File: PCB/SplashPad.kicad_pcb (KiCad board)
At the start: 2 copper layers, 67 x 83 mm, 58 parts, among them SW1 SW_Push_45deg, SW10 RotaryEncoder_Switch, SW2 SW_Push_45deg, SW3 SW_Push_45deg, SW4 SW_Push_45deg, SW5 SW_Push_45deg, SW6 SW_Push_45deg, SW7 SW_Push_45deg, SW8 SW_Push_45deg, SW9 SW_Push_45deg, U1 XIAO-RP2040-DIP

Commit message: Final Updates
This is the last one I swear
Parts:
- moved G*** 2.50 mm to (158.0, 146.5)
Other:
- board text added: "SplashPad"

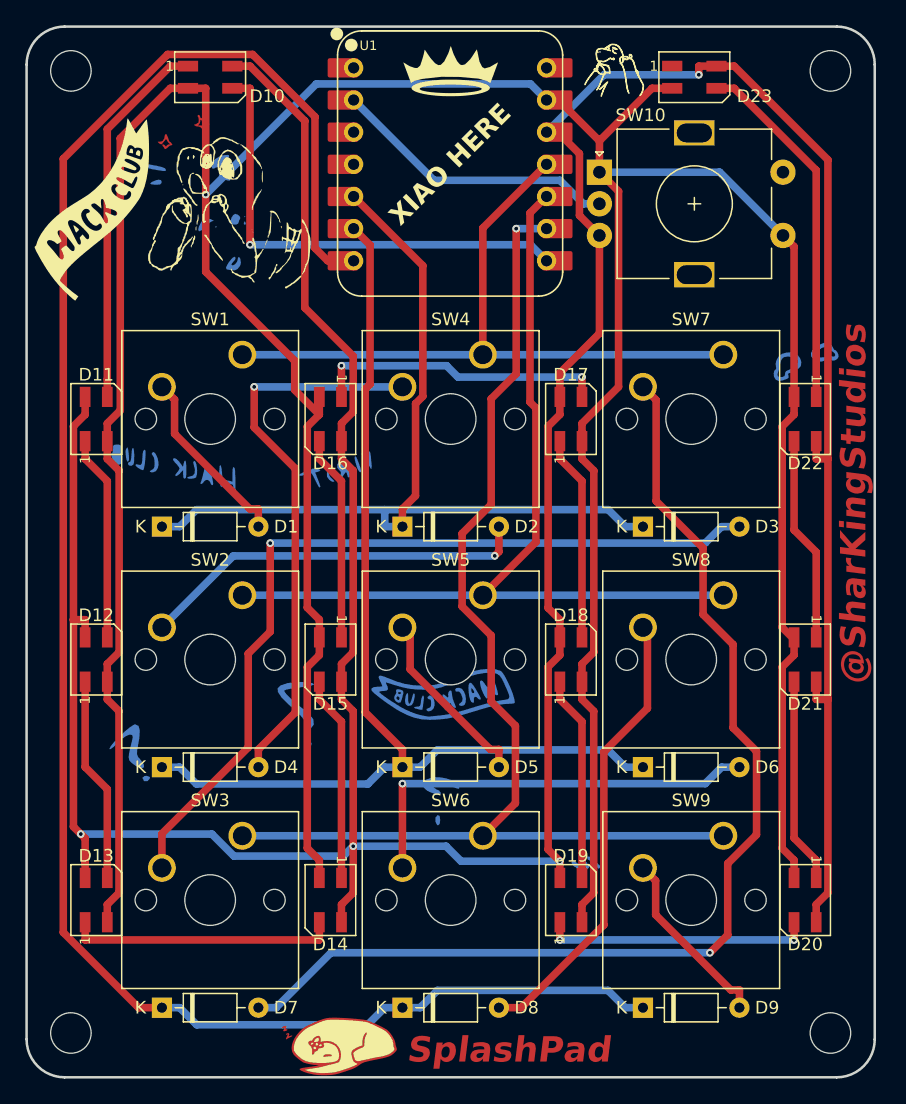
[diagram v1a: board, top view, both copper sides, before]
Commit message: LED Voltage Fix
I thought they worked at 3.3v oopsies
I also had the encoder wired wrong and fixed that.
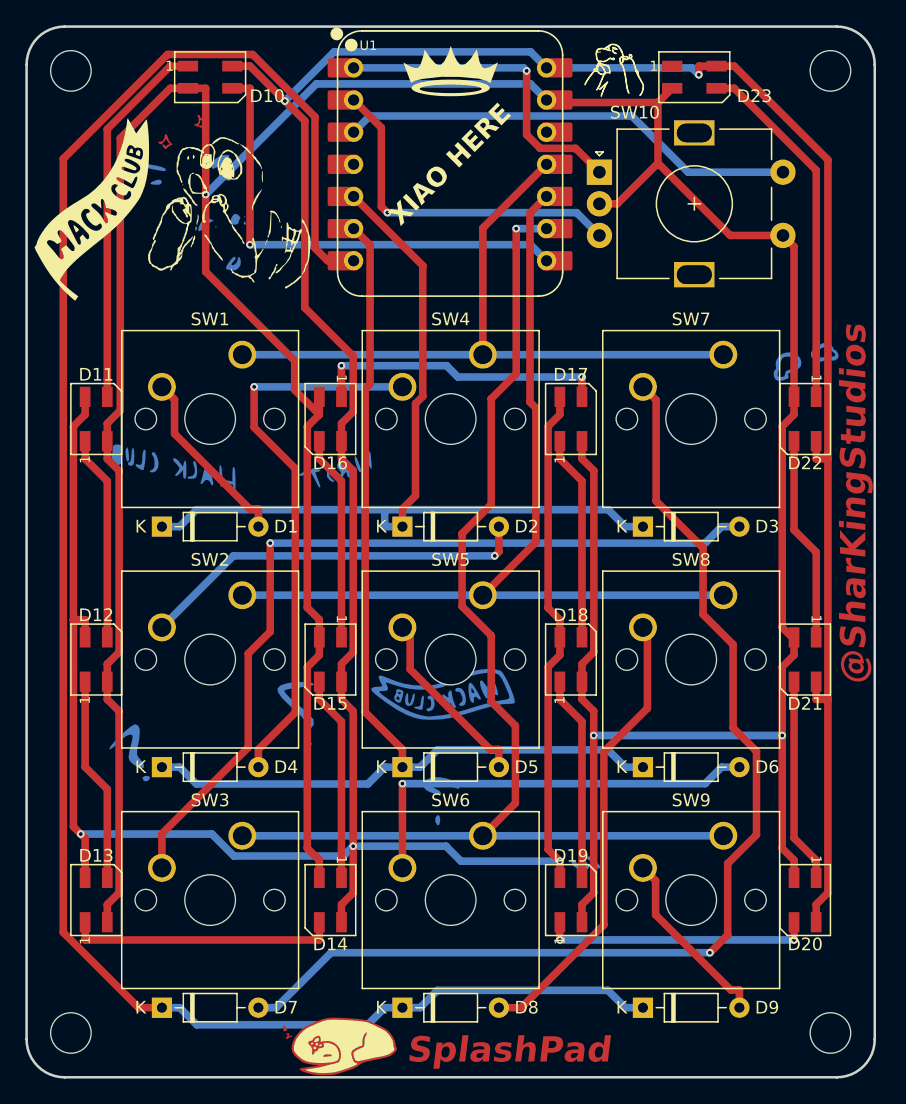
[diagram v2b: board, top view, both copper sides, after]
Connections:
- D10 pad 4: +3.3V -> +5V
- D11 pad 4: +3.3V -> +5V
- D12 pad 4: +3.3V -> +5V
- D13 pad 4: +3.3V -> +5V
- D14 pad 4: +3.3V -> +5V
- D15 pad 4: +3.3V -> +5V
- D16 pad 4: +3.3V -> +5V
- D17 pad 4: +3.3V -> +5V
- D18 pad 4: +3.3V -> +5V
- D19 pad 4: +3.3V -> +5V
- D20 pad 4: +3.3V -> +5V
- D21 pad 4: +3.3V -> +5V
- D22 pad 4: +3.3V -> +5V
- D23 pad 4: +3.3V -> +5V
- SW10 pad A: GND -> Pot Analog 1
- SW10 pad B: +3.3V -> Pot Analog 2
- SW10 pad C: Pot Analog 2 -> GND
- SW10 pad S2: Pot Button 2 -> Pot Button 1
- U1 pad 14: unconnected-(U1-VBUS-Pad14) -> +5V
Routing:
- net +3.3V: track 311.9 -> 0.89 mm, vias 4 -> 0
- net +5V: track 0.00 -> 309.4 mm, vias 0 -> 5
- net Pot Button 1: track 0.84 -> 37.1 mm
- net Pot Analog 1: track 0.84 -> 26.6 mm, vias 0 -> 1
- net GND: track 319.9 -> 314.1 mm, vias 1 -> 3
- net Pot Analog 2: track 23.6 -> 28.3 mm, vias 0 -> 1
- net unconnected-(U1-VBUS-Pad14): track 0.84 -> 0.00 mm
